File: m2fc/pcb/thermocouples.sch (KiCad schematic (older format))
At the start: 22 parts

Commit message: update more bits on flight computer..
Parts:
- removed IC? (x2): OP2177, symbol OP2177
- added C?: 1µ, 1206, symbol C
- added C? (x4): 100n, 1206, symbol C
- added C? (x2): 10µ, 1411, symbol CP1
- added C? (x2): 100n, 0603, symbol C
- added C? (x2): 10n, 0603, symbol C
- added IC? (x4): AD8656, SOIC8, symbol AD8656
- added IC?: AD8495, 8MSOP, symbol AD8495
- added P?: CONN_2, symbol CONN_2
- added R?: 1M, 0603, symbol R
- added R? (x2): 1k, 0603, symbol R
- added R?: 8.87k, 0603, symbol R
- added R?: 31.6k, 0603, symbol R
- added R?: 2.94k, 0603, symbol R
- added R?: 95.3k, 0603, symbol R
- added TP? (x4): TESTPAD, symbol TESTPAD
- C?: footprint (none) -> 1206; Farnell (none) -> 2362126
- C? (x2): footprint (none) -> 1206; Farnell (none) -> 2211074
- C? (x2): value C -> 10n; footprint (none) -> 0603; Farnell (none) -> 2112704
- C? (x2): value C -> 100n; footprint (none) -> 1206; Farnell (none) -> 2211074
- IC?: footprint (none) -> 8MSOP
- P?: Farnell (none) -> 3810628
- R?: footprint (none) -> 0603
- R? (x2): footprint (none) -> 0603; Farnell (none) -> 2116678
- R?: value R -> 8.87k; footprint (none) -> 0603; Farnell (none) -> 2116779
- R?: value R -> 31.6k; footprint (none) -> 0603; Farnell (none) -> 2116838
- R?: value R -> 2.94k; footprint (none) -> 0603; Farnell (none) -> 2117211
- R?: value R -> 95.3k; footprint (none) -> 0603; Farnell (none) -> 2117373
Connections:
- wire segments 66 -> 132
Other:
- note added: "FILTERING\n===============\nSignals of interest: 0 to 100Hz\nNyquist: 1kHz\nSample: 2kHz\n\nFRONTEND FILTER\n------------------\nFreq, Diff: 1/(2 pi R (2Cc + Cd)) = 132Hz\nFreq, CM: 1/(2 pi R Cc) = 1591Hz\n\nANTIALIAS FILTER\n------------------\n-3dB: 300Hz\nRejection at Nyquist: -40dB"
- note added: "THERMOCOUPLE 1"
- note added: "THERMOCOUPLE 2"
- note added: "THERMOCOUPLES"
- note removed: "FILTERING\n===============\nSignals of interest: 0 to 100Hz\nNyquist: 1kHz\nSample: 2kHz\n\nFRONTEND FILTER\n------------------\nFreq, Diff: 1/(2 pi R (2Cc + Cd)) = 132Hz\nFreq, CM: 1/(2 pi R Cc) = 1591Hz\n\nANTIALIAS FILTER\n------------------\nAA corner: 200Hz\nRejection at Nyquist:"
- moved on the sheet: C?, IC?, P?, R?

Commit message: everything... wired... up...
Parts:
- added C?: 1µ, 1206, symbol C
- added C? (x4): 100n, 1206, symbol C
- added C? (x2): 10µ, 1411, symbol CP1
- added C? (x2): 100n, 0603, symbol C
- added C? (x2): 10n, 0603, symbol C
- added IC?: AD8495, 8MSOP, symbol AD8495
- added IC? (x2): AD8656, SOIC8, symbol AD8656
- added P?: CONN_2, symbol CONN_2
- added R?: 1M, 0603, symbol R
- added R? (x2): 1k, 0603, symbol R
- added R?: 8.87k, 0603, symbol R
- added R?: 31.6k, 0603, symbol R
- added R?: 2.94k, 0603, symbol R
- added R?: 95.3k, 0603, symbol R
- added TP? (x2): TESTPAD, symbol TESTPAD
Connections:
- net labels added: THERMO_2, THERMO_3
- wire segments 132 -> 198
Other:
- moved on the sheet: C?, IC?, IC?A, IC?B, P?, R?, TP?

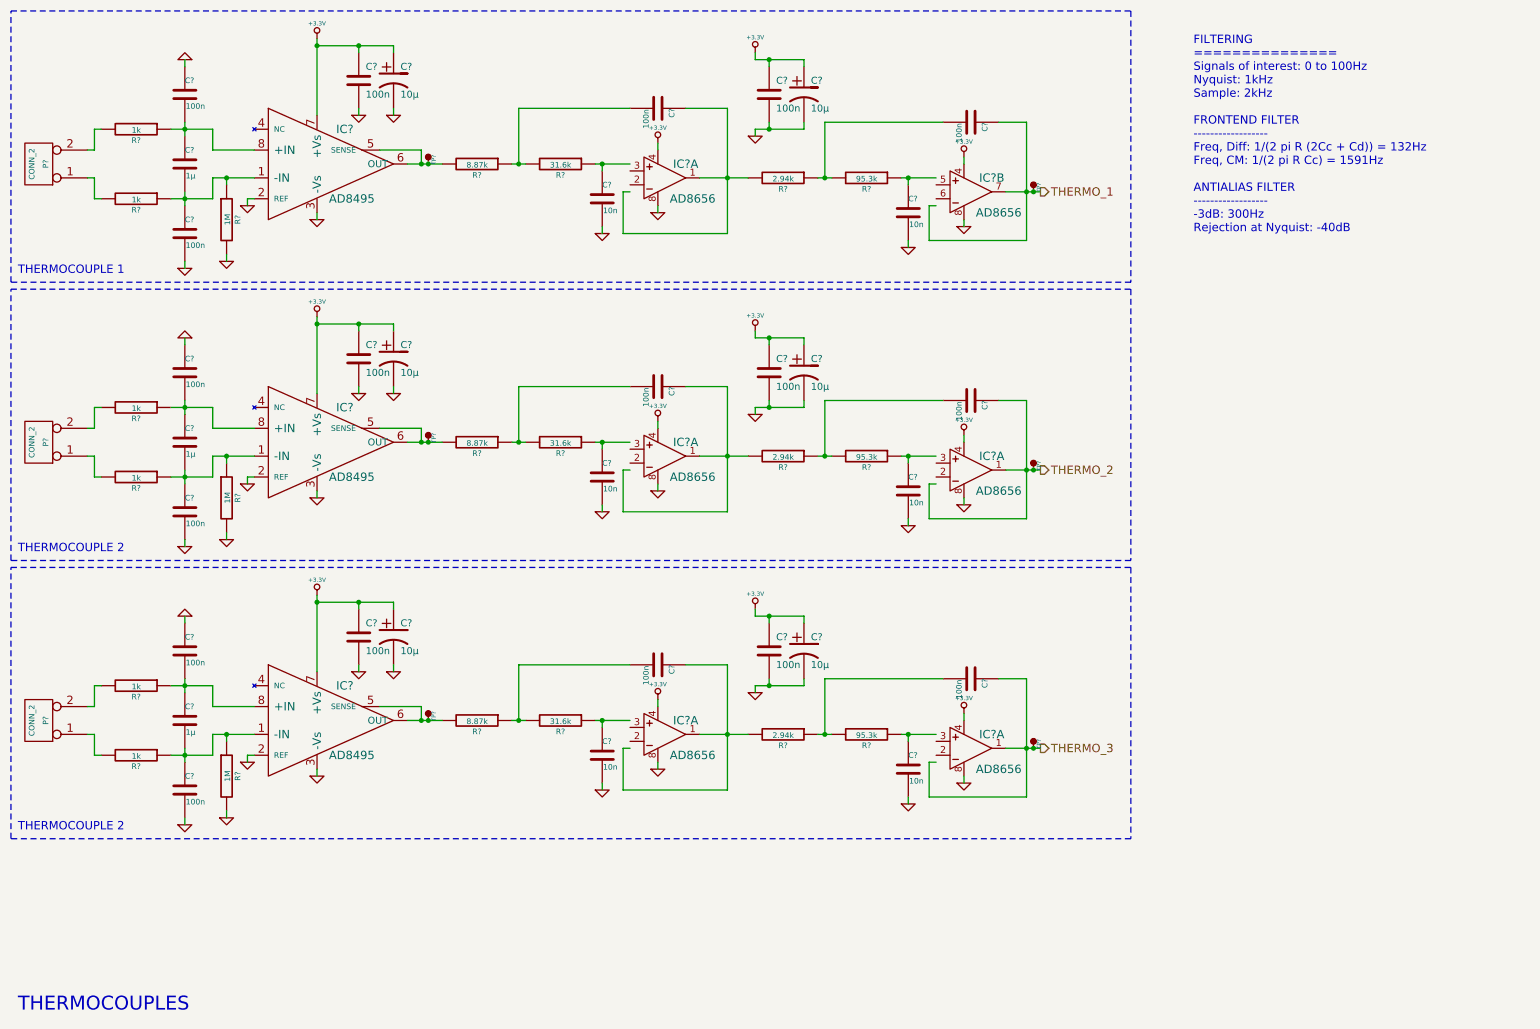
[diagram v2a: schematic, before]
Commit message: fix all the erc errors
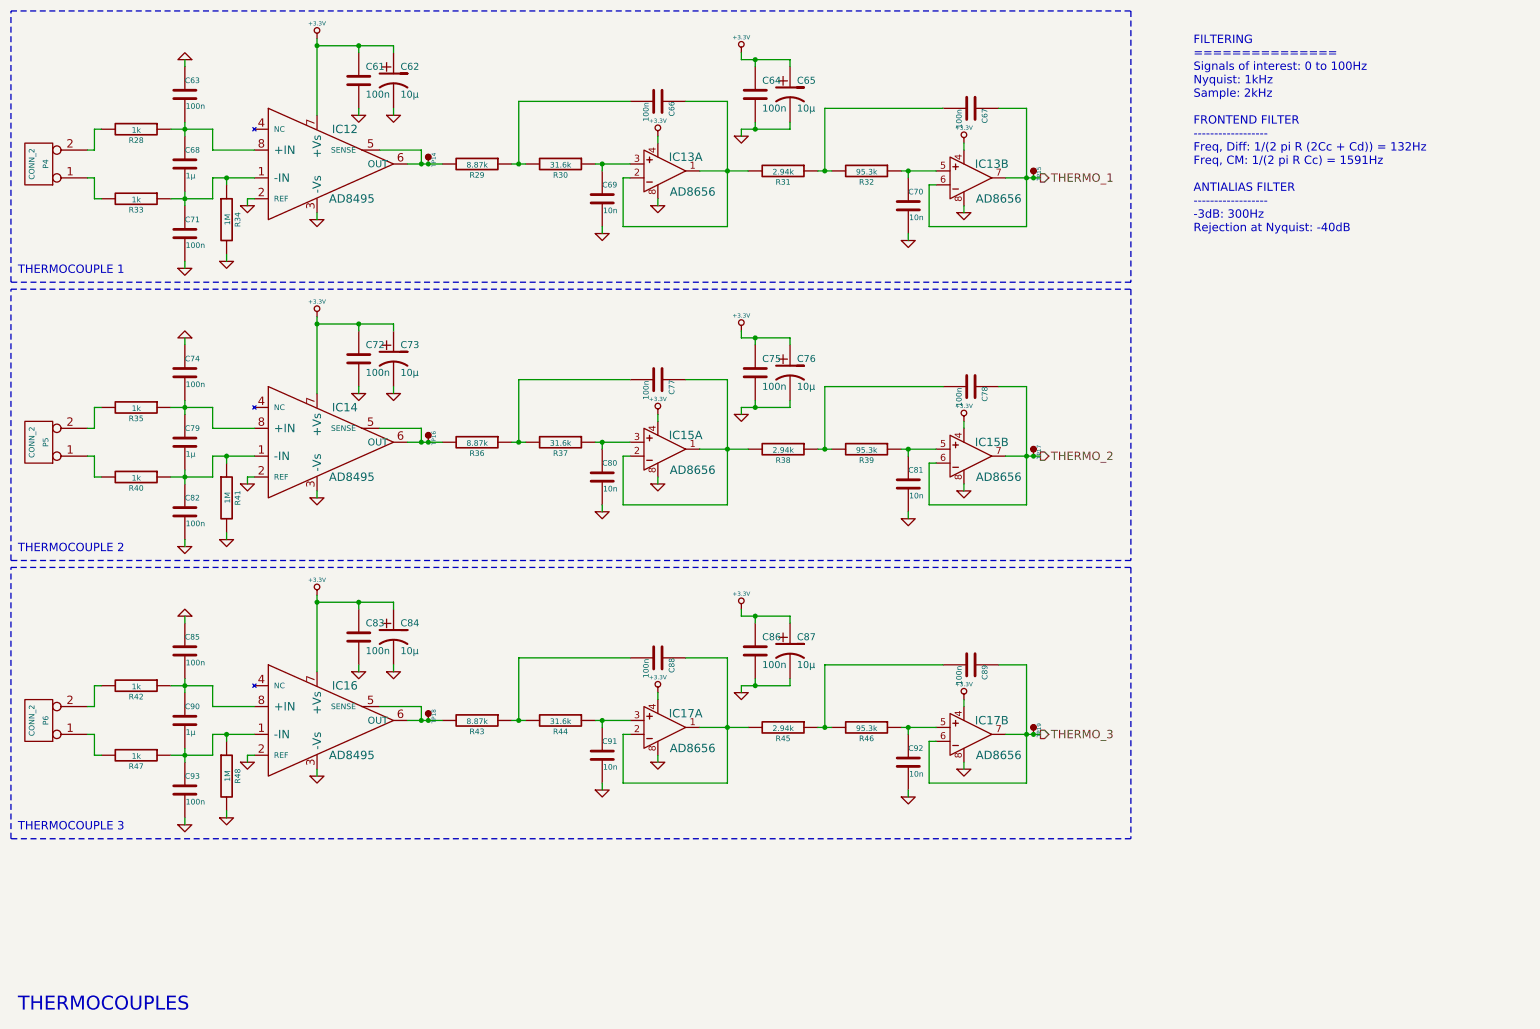
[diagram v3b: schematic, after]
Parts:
- removed C? (x2): 1µ, 1206, symbol C
- removed C? (x8): 100n, 1206, symbol C
- removed C? (x4): 10µ, 1411, symbol CP1
- removed C? (x4): 100n, 0603, symbol C
- removed C? (x4): 10n, 0603, symbol C
- removed IC? (x3): AD8495, 8MSOP, symbol AD8495
- removed IC? (x4): AD8656, SOIC8, symbol AD8656
- removed P? (x2): CONN_2, symbol CONN_2
- removed R? (x2): 1M, 0603, symbol R
- removed R? (x4): 1k, 0603, symbol R
- removed R? (x2): 8.87k, 0603, symbol R
- removed R? (x2): 31.6k, 0603, symbol R
- removed R? (x2): 2.94k, 0603, symbol R
- removed R? (x2): 95.3k, 0603, symbol R
- removed TP? (x4): TESTPAD, symbol TESTPAD
- added C72, C75, C83, C86: 100n, 0603, symbol C
- added C73, C76, C84, C87: 10µ, 1411, symbol CP1
- added C74, C77, C78, C82, C85, C88, C89, C93: 100n, 1206, symbol C
- added C79, C90: 1µ, 1206, symbol C
- added C80, C81, C91, C92: 10n, 0603, symbol C
- added IC12, IC14, IC16: AD8495, symbol AD8495
- added IC15, IC17: AD8656, SOIC8, symbol AD8656
- added P5, P6: CONN_2, symbol CONN_2
- added R35, R40, R42, R47: 1k, 0603, symbol R
- added R36, R43: 8.87k, 0603, symbol R
- added R37, R44: 31.6k, 0603, symbol R
- added R38, R45: 2.94k, 0603, symbol R
- added R39, R46: 95.3k, 0603, symbol R
- added R41, R48: 1M, 0603, symbol R
- added TP16, TP17, TP18, TP19: TESTPAD, symbol TESTPAD
- gave numbers to parts that had none: 22
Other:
- note added: "THERMOCOUPLE 3"
- moved on the sheet: C64, C65, C66, C67, C70, IC13A, IC13B, R31, R32, TP15

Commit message: add missing farnell numbers
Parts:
- IC12, IC14, IC16: footprint (none) -> 8MSOP; Farnell (none) -> 2067807
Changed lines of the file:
@@
 F 0 "IC12" H 2900 1850 60  0000 C CNN
 F 1 "AD8495" H 2950 1350 60  0000 C CNN
-F 2 "" H 2700 1600 60  0000 C CNN
+F 2 "8MSOP" H 2700 1600 60  0001 C CNN
 F 3 "" H 2700 1600 60  0000 C CNN
+F 4 "2067807" H 2700 1600 60  0001 C CNN "Farnell"
 	1    2700 1600
 	1    0    0    -1
@@
 F 0 "IC14" H 2900 3850 60  0000 C CNN
 F 1 "AD8495" H 2950 3350 60  0000 C CNN
-F 2 "" H 2700 3600 60  0000 C CNN
+F 2 "8MSOP" H 2700 3600 60  0001 C CNN
 F 3 "" H 2700 3600 60  0000 C CNN
+F 4 "2067807" H 2700 3600 60  0001 C CNN "Farnell"
 	1    2700 3600
 	1    0    0    -1
@@
 F 0 "IC16" H 2900 5850 60  0000 C CNN
 F 1 "AD8495" H 2950 5350 60  0000 C CNN
-F 2 "" H 2700 5600 60  0000 C CNN
+F 2 "8MSOP" H 2700 5600 60  0001 C CNN
 F 3 "" H 2700 5600 60  0000 C CNN
+F 4 "2067807" H 2700 5600 60  0001 C CNN "Farnell"
 	1    2700 5600
 	1    0    0    -1

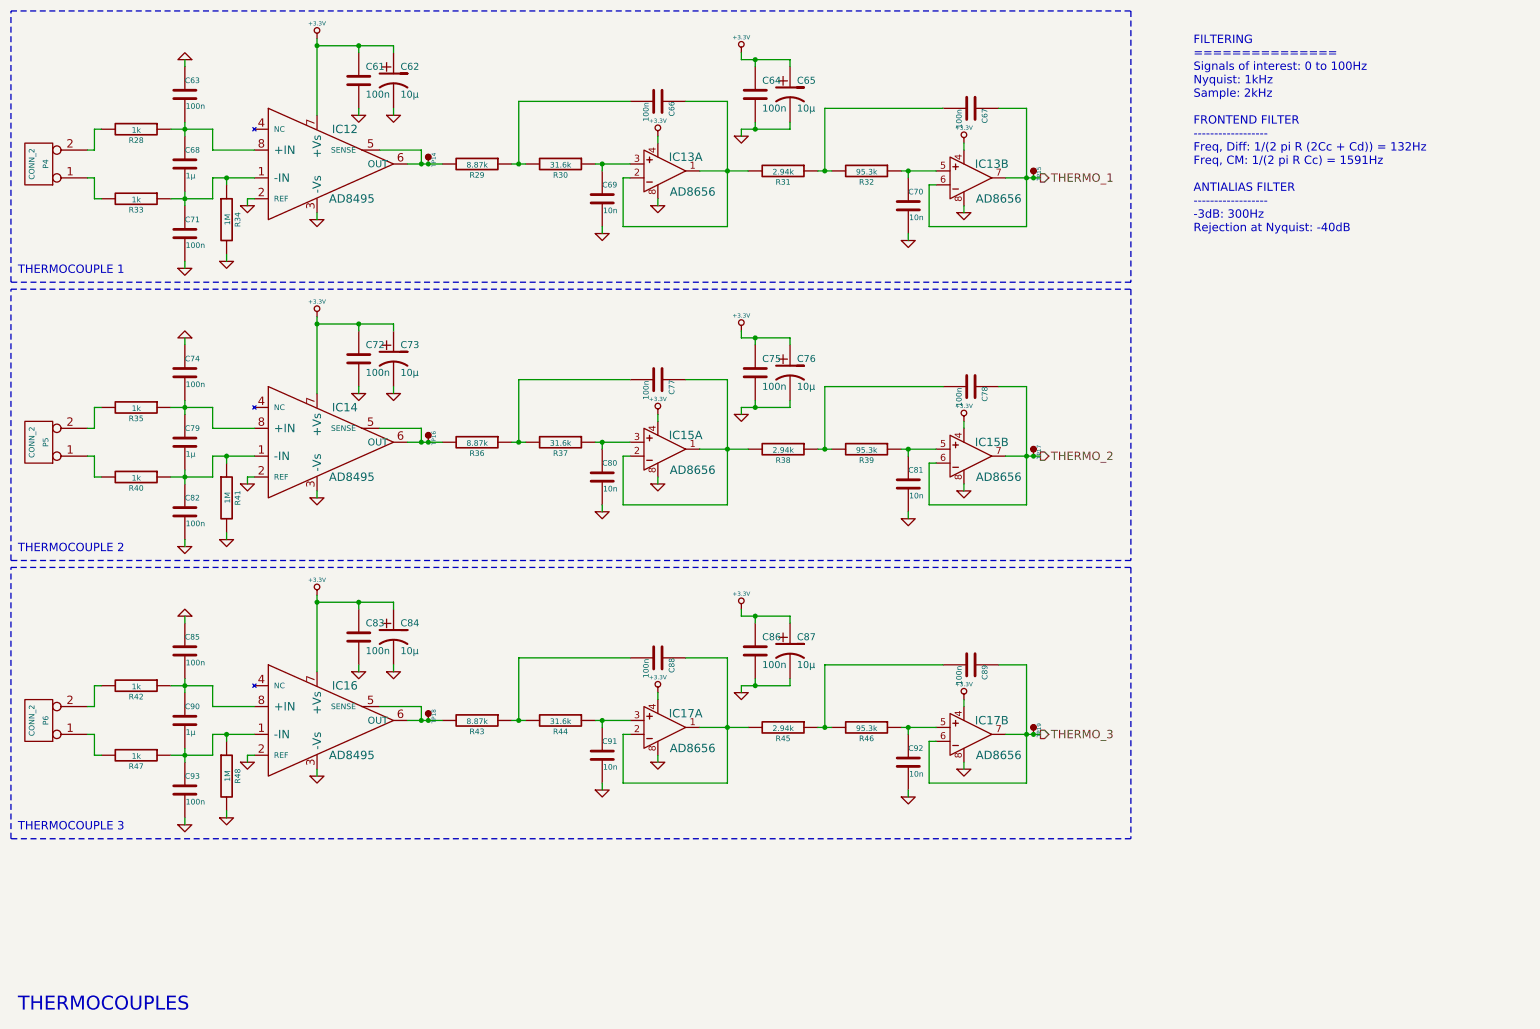
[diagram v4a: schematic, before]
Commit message: update m2fc sch with 3rd pyro and SJs
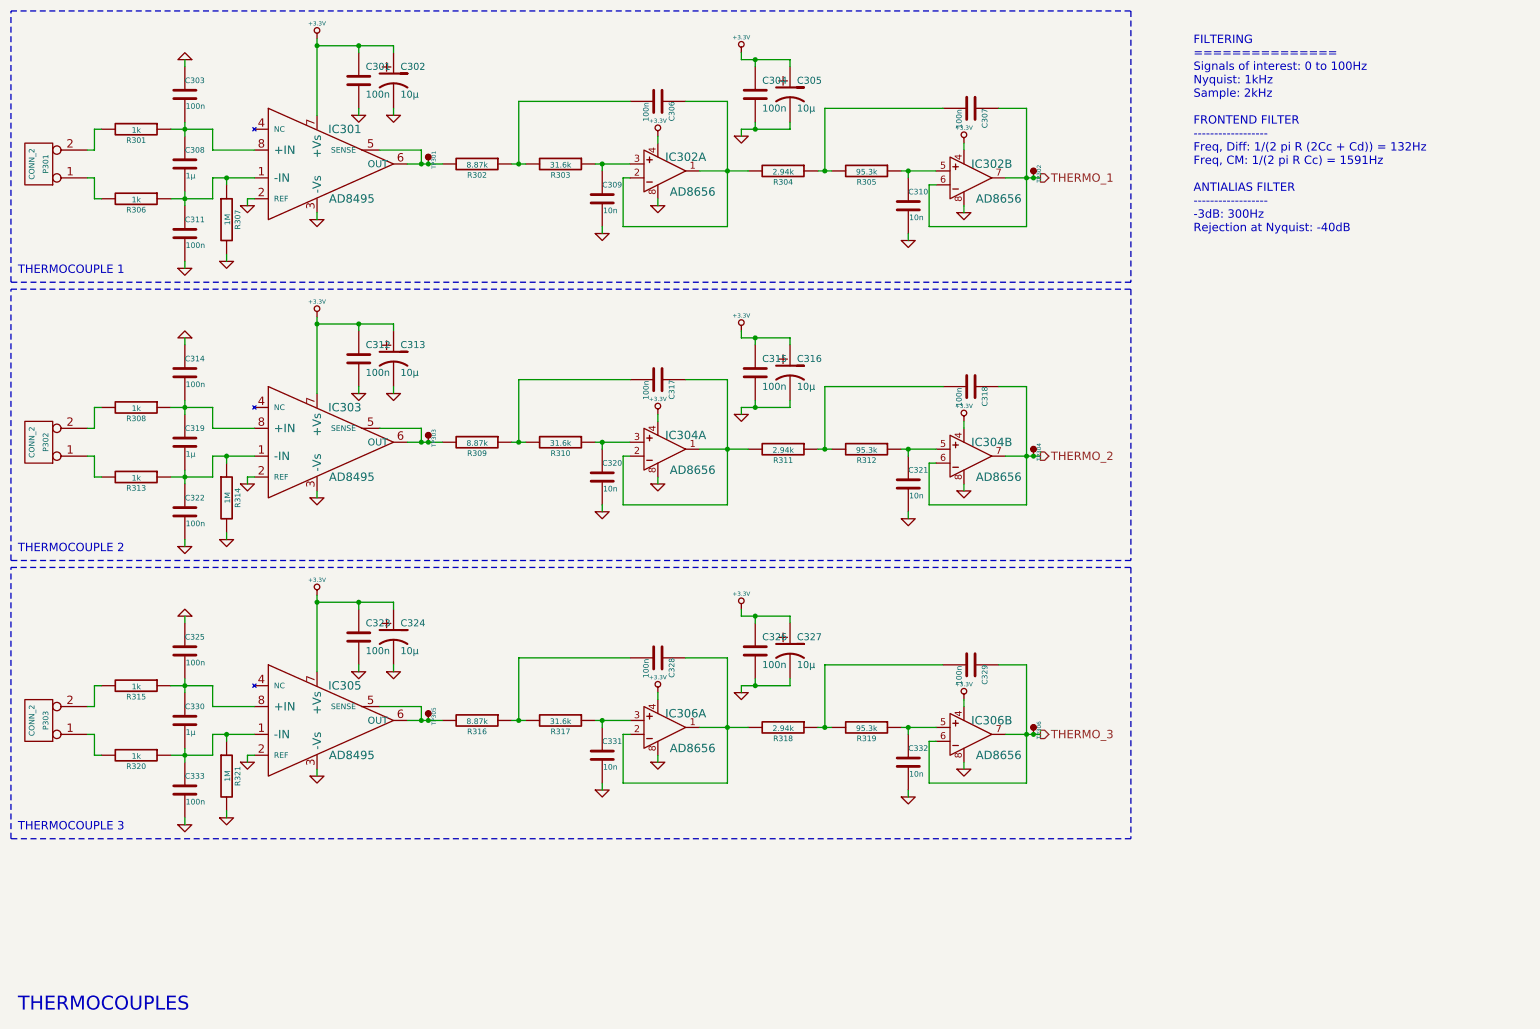
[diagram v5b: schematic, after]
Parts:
- renumbered C61 to C301, C62 to C302, C63 to C303, C64 to C304, C65 to C305, C66 to C306, C67 to C307, C68 to C308, C69 to C309, C70 to C310, C71 to C311, C72 to C312, C73 to C313, C74 to C314, C75 to C315, C76 to C316, C77 to C317, C78 to C318, C79 to C319, C80 to C320, C81 to C321, C82 to C322, C83 to C323, C84 to C324, C85 to C325, C86 to C326, C87 to C327, C88 to C328, C89 to C329, C90 to C330, C91 to C331, C92 to C332, C93 to C333, IC12 to IC301, IC13 to IC302, IC14 to IC303, IC15 to IC304, IC16 to IC305, IC17 to IC306, P4 to P301, P5 to P302, P6 to P303, R28 to R301, R29 to R302, R30 to R303, R31 to R304, R32 to R305, R33 to R306, R34 to R307, R35 to R308, R36 to R309, R37 to R310, R38 to R311, R39 to R312, R40 to R313, R41 to R314, R42 to R315, R43 to R316, R44 to R317, R45 to R318, R46 to R319, R47 to R320, R48 to R321, TP14 to TP301, TP15 to TP302, TP16 to TP303, TP17 to TP304, TP18 to TP305, TP19 to TP306

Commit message: quick go at wiring diagram
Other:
- note added: "MAYBE ADD SHIELD\nCONNECTOR"
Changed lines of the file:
@@
 	1    0    0    -1
 $EndComp
+Text Notes 700  1150 0    60   ~ 0
+MAYBE ADD SHIELD\nCONNECTOR
 $EndSCHEMATC
